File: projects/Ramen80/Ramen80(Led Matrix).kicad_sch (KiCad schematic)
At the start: 113 parts, among them U2 IS31FL3733-TQ, U3 IS31FL3733-TQ

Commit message: Fixing the broke stuff
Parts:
- C10, C14, C8: value 0.1f -> 0.47f
- C13, C5, C9: value 0.47f -> 0.1u
- C15, C18, C7: value 0.47f -> 0.1f
- C16: value 0.1f -> 1u
- C4: value 0.1f -> 4.7u
- R1: value 100k -> 5k1
- R2: value 20k -> 22
- R3: value 2k -> 5k1
- R4: value 2k -> 22
- R5: value 100k -> 10k
- R6: value 20k -> 10k
- renumbered LED18 to LED10, LED19 to LED11, LED20 to LED12, LED21 to LED13, LED22 to LED14, LED23 to LED15, LED24 to LED16, LED34 to LED17, LED35 to LED18, LED36 to LED19, LED37 to LED20, LED38 to LED21, LED39 to LED22, LED40 to LED23, LED41 to LED24, LED51 to LED25, LED52 to LED26, LED53 to LED27, LED54 to LED28, LED55 to LED29, LED56 to LED30, LED57 to LED31, LED58 to LED32, LED64 to LED33, LED65 to LED34, LED66 to LED35, LED67 to LED36, LED68 to LED37, LED69 to LED38, LED70 to LED39, LED71 to LED40, LED77 to LED41, LED78 to LED42, LED79 to LED43, LED80 to LED44, LED9 to LED45, LED10 to LED46, LED11 to LED47, LED12 to LED48, LED13 to LED49, LED14 to LED50, LED15 to LED51, LED16 to LED52, LED25 to LED53, LED26 to LED54, LED27 to LED55, LED28 to LED56, LED29 to LED57, LED30 to LED58, LED31 to LED59, LED32 to LED60, LED42 to LED61, LED43 to LED62, LED44 to LED63, LED45 to LED64, LED46 to LED65, LED47 to LED66, LED48 to LED67, LED49 to LED68, LED59 to LED69, LED60 to LED70, LED61 to LED71, LED62 to LED72, LED63 to LED73, LED33 to LED74, LED50 to LED75, LED72 to LED76, LED73 to LED77, LED74 to LED78, LED75 to LED79, LED76 to LED80, LED17 to LED9

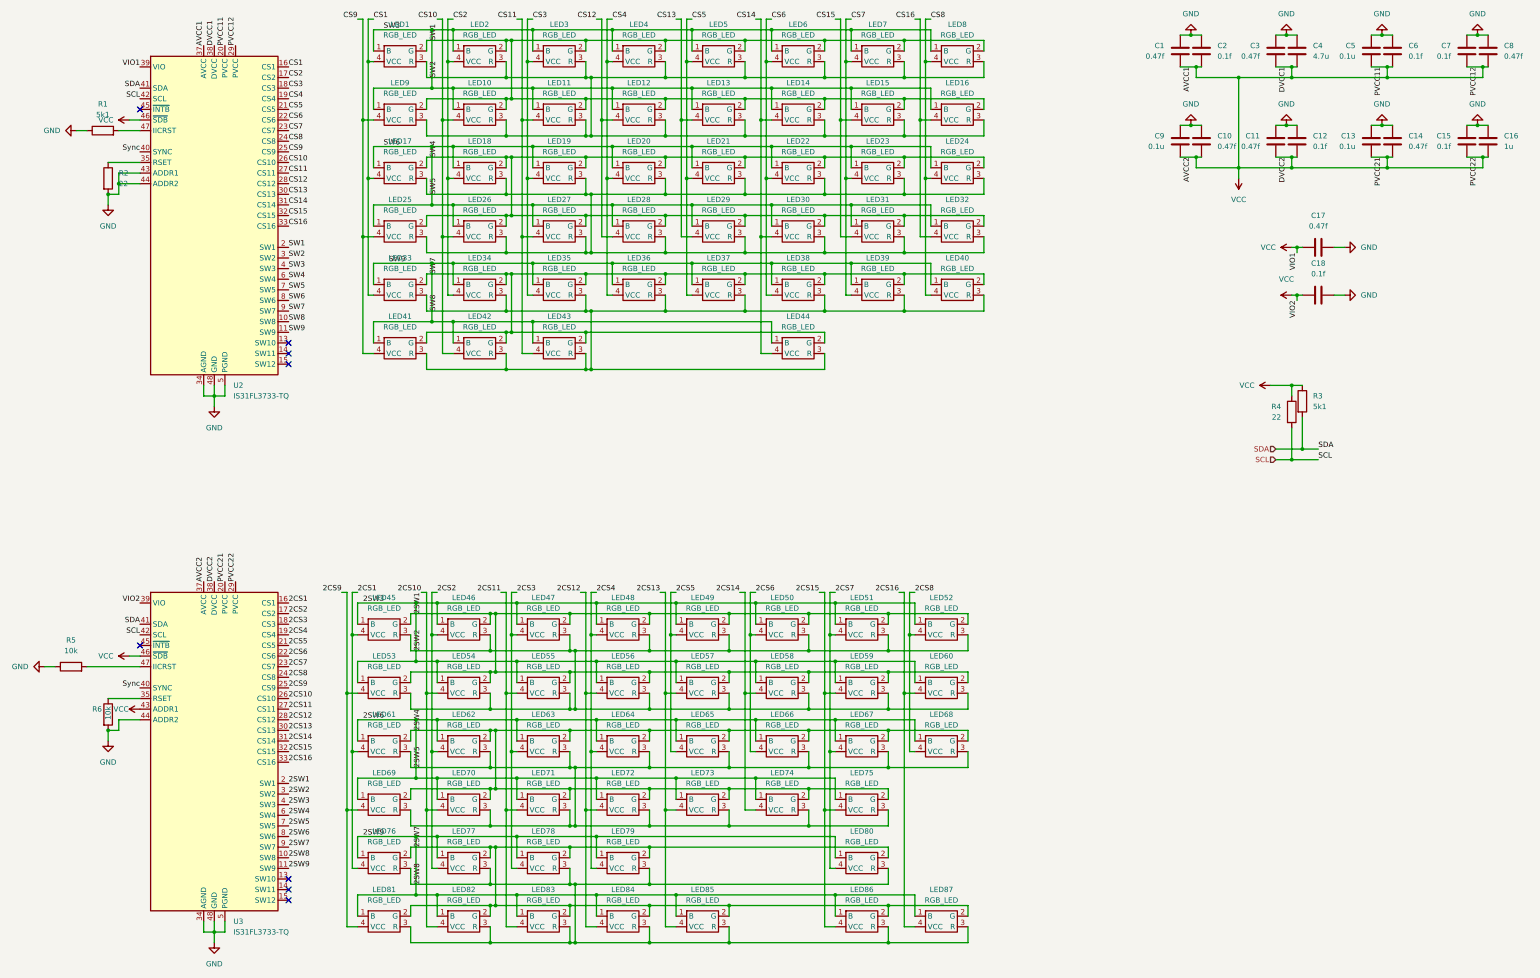
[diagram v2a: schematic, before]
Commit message: Fixes (re-mapped pinout)
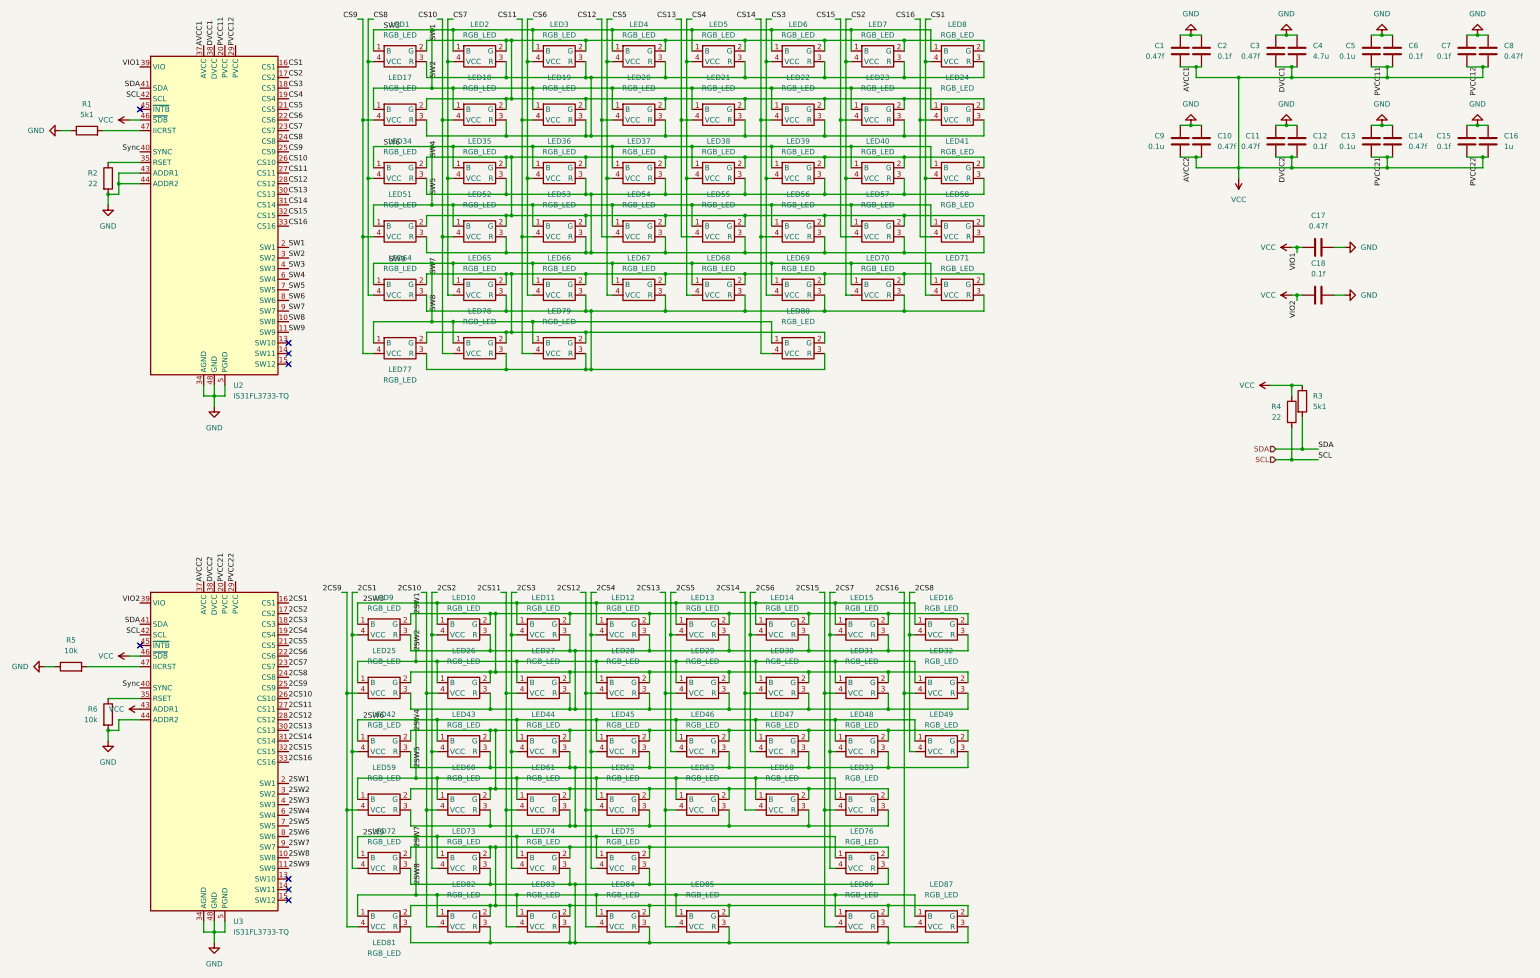
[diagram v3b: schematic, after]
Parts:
- removed LED17, LED18, LED19, LED20, LED21, LED22, LED23, LED24: RGB_LED, RamenKeebs:QBLP677R-RGB, symbol RamenKeebs:RGB_LED
- added LED10, LED11, LED12, LED13, LED14, LED15, LED16, LED9: RGB_LED, RamenKeebs:QBLP677R-RGB, symbol RamenKeebs:RGB_LED
- renumbered LED9 to LED17, LED10 to LED18, LED11 to LED19, LED12 to LED20, LED13 to LED21, LED14 to LED22, LED15 to LED23, LED16 to LED24
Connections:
- net 2CS1: now also LED42.4 (VCC), LED72.4 (VCC), LED9.4 (VCC); no longer LED45.4 (VCC), LED61.4 (VCC), LED76.4 (VCC)
- net 2CS10: now also LED26.4 (VCC), LED60.4 (VCC); no longer LED54.4 (VCC), LED70.4 (VCC)
- net 2CS11: now also LED27.4 (VCC), LED61.4 (VCC); no longer LED55.4 (VCC), LED71.4 (VCC)
- net 2CS12: now also LED28.4 (VCC), LED62.4 (VCC); no longer LED56.4 (VCC), LED72.4 (VCC)
- net 2CS13: now also LED29.4 (VCC), LED63.4 (VCC); no longer LED57.4 (VCC), LED73.4 (VCC)
- net 2CS14: now also LED30.4 (VCC), LED50.4 (VCC); no longer LED58.4 (VCC), LED74.4 (VCC)
- net 2CS15: now also LED31.4 (VCC), LED33.4 (VCC); no longer LED59.4 (VCC), LED75.4 (VCC)
- net 2CS16: now also LED32.4 (VCC); no longer LED60.4 (VCC)
- net 2CS2: now also LED43.4 (VCC), LED73.4 (VCC), LED10.4 (VCC); no longer LED46.4 (VCC), LED62.4 (VCC), LED77.4 (VCC)
- net 2CS3: now also LED44.4 (VCC), LED74.4 (VCC), LED11.4 (VCC); no longer LED47.4 (VCC), LED63.4 (VCC), LED78.4 (VCC)
- net 2CS4: now also LED45.4 (VCC), LED75.4 (VCC), LED12.4 (VCC); no longer LED48.4 (VCC), LED64.4 (VCC), LED79.4 (VCC)
- net 2CS5: now also LED46.4 (VCC), LED13.4 (VCC); no longer LED49.4 (VCC), LED65.4 (VCC)
- net 2CS6: now also LED47.4 (VCC), LED14.4 (VCC); no longer LED50.4 (VCC), LED66.4 (VCC)
- net 2CS7: now also LED48.4 (VCC), LED76.4 (VCC), LED15.4 (VCC); no longer LED51.4 (VCC), LED67.4 (VCC), LED80.4 (VCC)
- net 2CS8: now also LED49.4 (VCC), LED16.4 (VCC); no longer LED52.4 (VCC), LED68.4 (VCC)
- net 2CS9 : now also LED25.4 (VCC), LED59.4 (VCC); no longer LED53.4 (VCC), LED69.4 (VCC)
- net 2SW1: now also LED25.2 (G), LED26.2 (G), LED27.2 (G), LED28.2 (G), LED29.2 (G), LED30.2 (G), LED31.2 (G), LED32.2 (G), LED10.2 (G), LED11.2 (G), LED12.2 (G), LED13.2 (G), LED14.2 (G), LED15.2 (G), LED16.2 (G), LED9.2 (G); no longer LED45.2 (G), LED46.2 (G), LED47.2 (G), LED48.2 (G), LED49.2 (G), LED50.2 (G), LED51.2 (G), LED52.2 (G), LED53.2 (G), LED54.2 (G), LED55.2 (G), LED56.2 (G), LED57.2 (G), LED58.2 (G), LED59.2 (G), LED60.2 (G)
- net 2SW2: now also LED25.3 (R), LED26.3 (R), LED27.3 (R), LED28.3 (R), LED29.3 (R), LED30.3 (R), LED31.3 (R), LED32.3 (R), LED10.3 (R), LED11.3 (R), LED12.3 (R), LED13.3 (R), LED14.3 (R), LED15.3 (R), LED16.3 (R), LED9.3 (R); no longer LED45.3 (R), LED46.3 (R), LED47.3 (R), LED48.3 (R), LED49.3 (R), LED50.3 (R), LED51.3 (R), LED52.3 (R), LED53.3 (R), LED54.3 (R), LED55.3 (R), LED56.3 (R), LED57.3 (R), LED58.3 (R), LED59.3 (R), LED60.3 (R)
- net 2SW3: now also LED25.1 (B), LED26.1 (B), LED27.1 (B), LED28.1 (B), LED29.1 (B), LED30.1 (B), LED31.1 (B), LED32.1 (B), LED10.1 (B), LED11.1 (B), LED12.1 (B), LED13.1 (B), LED14.1 (B), LED15.1 (B), LED16.1 (B), LED9.1 (B); no longer LED45.1 (B), LED46.1 (B), LED47.1 (B), LED48.1 (B), LED49.1 (B), LED50.1 (B), LED51.1 (B), LED52.1 (B), LED53.1 (B), LED54.1 (B), LED55.1 (B), LED56.1 (B), LED57.1 (B), LED58.1 (B), LED59.1 (B), LED60.1 (B)
- net 2SW4: now also LED33.2 (G), LED42.2 (G), LED43.2 (G), LED44.2 (G), LED45.2 (G), LED46.2 (G), LED47.2 (G), LED48.2 (G), LED49.2 (G), LED50.2 (G), LED59.2 (G), LED60.2 (G); no longer LED64.2 (G), LED65.2 (G), LED66.2 (G), LED67.2 (G), LED68.2 (G), LED69.2 (G), LED70.2 (G), LED71.2 (G), LED72.2 (G), LED73.2 (G), LED74.2 (G), LED75.2 (G)
- net 2SW5: now also LED33.3 (R), LED42.3 (R), LED43.3 (R), LED44.3 (R), LED45.3 (R), LED46.3 (R), LED47.3 (R), LED48.3 (R), LED49.3 (R), LED50.3 (R), LED59.3 (R), LED60.3 (R); no longer LED64.3 (R), LED65.3 (R), LED66.3 (R), LED67.3 (R), LED68.3 (R), LED69.3 (R), LED70.3 (R), LED71.3 (R), LED72.3 (R), LED73.3 (R), LED74.3 (R), LED75.3 (R)
- net 2SW6: now also LED33.1 (B), LED42.1 (B), LED43.1 (B), LED44.1 (B), LED45.1 (B), LED46.1 (B), LED47.1 (B), LED48.1 (B), LED49.1 (B), LED50.1 (B), LED59.1 (B), LED60.1 (B); no longer LED64.1 (B), LED65.1 (B), LED66.1 (B), LED67.1 (B), LED68.1 (B), LED69.1 (B), LED70.1 (B), LED71.1 (B), LED72.1 (B), LED73.1 (B), LED74.1 (B), LED75.1 (B)
- net 2SW7: now also LED72.2 (G), LED73.2 (G), LED74.2 (G), LED75.2 (G); no longer LED77.2 (G), LED78.2 (G), LED79.2 (G), LED80.2 (G)
- net 2SW8: now also LED72.3 (R), LED73.3 (R), LED74.3 (R), LED75.3 (R); no longer LED77.3 (R), LED78.3 (R), LED79.3 (R), LED80.3 (R)
- net 2SW9: now also LED72.1 (B), LED73.1 (B), LED74.1 (B), LED75.1 (B); no longer LED77.1 (B), LED78.1 (B), LED79.1 (B), LED80.1 (B)
- net CS1: now also LED41.4 (VCC), LED71.4 (VCC), LED8.4 (VCC); no longer LED1.4 (VCC), LED33.4 (VCC)
- net CS10: now also LED52.4 (VCC), LED78.4 (VCC); no longer LED26.4 (VCC), LED42.4 (VCC)
- net CS11: now also LED53.4 (VCC), LED79.4 (VCC); no longer LED27.4 (VCC), LED43.4 (VCC)
- net CS12: now also LED54.4 (VCC); no longer LED28.4 (VCC)
- net CS13: now also LED55.4 (VCC); no longer LED29.4 (VCC)
- net CS14: now also LED56.4 (VCC), LED80.4 (VCC); no longer LED30.4 (VCC), LED44.4 (VCC)
- net CS15: now also LED57.4 (VCC); no longer LED31.4 (VCC)
- net CS16: now also LED58.4 (VCC); no longer LED32.4 (VCC)
- net CS2: now also LED40.4 (VCC), LED7.4 (VCC), LED70.4 (VCC); no longer LED2.4 (VCC), LED34.4 (VCC)
- net CS3: now also LED39.4 (VCC), LED6.4 (VCC), LED69.4 (VCC); no longer LED3.4 (VCC), LED35.4 (VCC)
- net CS4: now also LED38.4 (VCC), LED5.4 (VCC), LED68.4 (VCC); no longer LED36.4 (VCC), LED4.4 (VCC)
- net CS5: now also LED4.4 (VCC), LED67.4 (VCC); no longer LED5.4 (VCC)
- net CS6: now also LED3.4 (VCC), LED36.4 (VCC), LED66.4 (VCC); no longer LED38.4 (VCC), LED6.4 (VCC)
- net CS7: now also LED2.4 (VCC), LED35.4 (VCC), LED65.4 (VCC); no longer LED39.4 (VCC), LED7.4 (VCC)
- net CS8: now also LED1.4 (VCC), LED34.4 (VCC), LED64.4 (VCC); no longer LED40.4 (VCC), LED8.4 (VCC)
- net CS9 : now also LED51.4 (VCC), LED77.4 (VCC); no longer LED25.4 (VCC), LED41.4 (VCC)
- net SW4: now also LED34.2 (G), LED35.2 (G), LED36.2 (G), LED37.2 (G), LED38.2 (G), LED39.2 (G), LED40.2 (G), LED41.2 (G), LED51.2 (G), LED52.2 (G), LED53.2 (G), LED54.2 (G), LED55.2 (G), LED56.2 (G), LED57.2 (G), LED58.2 (G); no longer LED25.2 (G), LED26.2 (G), LED27.2 (G), LED28.2 (G), LED29.2 (G), LED30.2 (G), LED31.2 (G), LED32.2 (G)
- net SW5: now also LED34.3 (R), LED35.3 (R), LED36.3 (R), LED37.3 (R), LED38.3 (R), LED39.3 (R), LED40.3 (R), LED41.3 (R), LED51.3 (R), LED52.3 (R), LED53.3 (R), LED54.3 (R), LED55.3 (R), LED56.3 (R), LED57.3 (R), LED58.3 (R); no longer LED25.3 (R), LED26.3 (R), LED27.3 (R), LED28.3 (R), LED29.3 (R), LED30.3 (R), LED31.3 (R), LED32.3 (R)
- net SW6: now also LED34.1 (B), LED35.1 (B), LED36.1 (B), LED37.1 (B), LED38.1 (B), LED39.1 (B), LED40.1 (B), LED41.1 (B), LED51.1 (B), LED52.1 (B), LED53.1 (B), LED54.1 (B), LED55.1 (B), LED56.1 (B), LED57.1 (B), LED58.1 (B); no longer LED25.1 (B), LED26.1 (B), LED27.1 (B), LED28.1 (B), LED29.1 (B), LED30.1 (B), LED31.1 (B), LED32.1 (B)
- net SW7: now also LED64.2 (G), LED65.2 (G), LED66.2 (G), LED67.2 (G), LED68.2 (G), LED69.2 (G), LED70.2 (G), LED71.2 (G), LED77.2 (G), LED78.2 (G), LED79.2 (G), LED80.2 (G); no longer LED33.2 (G), LED34.2 (G), LED35.2 (G), LED36.2 (G), LED37.2 (G), LED38.2 (G), LED39.2 (G), LED40.2 (G), LED41.2 (G), LED42.2 (G), LED43.2 (G), LED44.2 (G)
- net SW8: now also LED64.3 (R), LED65.3 (R), LED66.3 (R), LED67.3 (R), LED68.3 (R), LED69.3 (R), LED70.3 (R), LED71.3 (R), LED77.3 (R), LED78.3 (R), LED79.3 (R), LED80.3 (R); no longer LED33.3 (R), LED34.3 (R), LED35.3 (R), LED36.3 (R), LED37.3 (R), LED38.3 (R), LED39.3 (R), LED40.3 (R), LED41.3 (R), LED42.3 (R), LED43.3 (R), LED44.3 (R)
- net SW9 : now also LED64.1 (B), LED65.1 (B), LED66.1 (B), LED67.1 (B), LED68.1 (B), LED69.1 (B), LED70.1 (B), LED71.1 (B), LED77.1 (B), LED78.1 (B), LED79.1 (B), LED80.1 (B); no longer LED33.1 (B), LED34.1 (B), LED35.1 (B), LED36.1 (B), LED37.1 (B), LED38.1 (B), LED39.1 (B), LED40.1 (B), LED41.1 (B), LED42.1 (B), LED43.1 (B), LED44.1 (B)
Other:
- moved on the sheet: R1

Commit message: Final Fixes
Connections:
- net 2CS1: now also LED16.4 (VCC), LED49.4 (VCC); no longer LED42.4 (VCC), LED72.4 (VCC), LED9.4 (VCC)
- net 2CS10: now also LED30.4 (VCC), LED50.4 (VCC); no longer LED26.4 (VCC), LED60.4 (VCC), LED82.4 (VCC)
- net 2CS12: now also LED29.4 (VCC), LED63.4 (VCC), LED85.4 (VCC); no longer LED28.4 (VCC), LED62.4 (VCC), LED84.4 (VCC)
- net 2CS13: now also LED26.4 (VCC), LED60.4 (VCC), LED82.4 (VCC); no longer LED29.4 (VCC), LED63.4 (VCC), LED85.4 (VCC)
- net 2CS14: now also LED31.4 (VCC), LED33.4 (VCC), LED86.4 (VCC); no longer LED30.4 (VCC), LED50.4 (VCC)
- net 2CS15: now also LED25.4 (VCC), LED59.4 (VCC), LED81.4 (VCC); no longer LED31.4 (VCC), LED33.4 (VCC), LED86.4 (VCC)
- net 2CS2: now also LED11.4 (VCC), LED44.4 (VCC), LED74.4 (VCC); no longer LED10.4 (VCC), LED43.4 (VCC), LED73.4 (VCC)
- net 2CS3: now also LED15.4 (VCC), LED48.4 (VCC), LED76.4 (VCC); no longer LED11.4 (VCC), LED44.4 (VCC), LED74.4 (VCC)
- net 2CS4: now also LED14.4 (VCC), LED47.4 (VCC); no longer LED12.4 (VCC), LED45.4 (VCC), LED75.4 (VCC)
- net 2CS5: now also LED10.4 (VCC), LED43.4 (VCC), LED73.4 (VCC); no longer LED13.4 (VCC), LED46.4 (VCC)
- net 2CS6: now also LED13.4 (VCC), LED46.4 (VCC); no longer LED14.4 (VCC), LED47.4 (VCC)
- net 2CS7: now also LED12.4 (VCC), LED45.4 (VCC), LED75.4 (VCC); no longer LED15.4 (VCC), LED48.4 (VCC), LED76.4 (VCC)
- net 2CS8: now also LED42.4 (VCC), LED72.4 (VCC), LED9.4 (VCC); no longer LED16.4 (VCC), LED49.4 (VCC)
- net 2CS9 : now also LED28.4 (VCC), LED62.4 (VCC), LED84.4 (VCC); no longer LED25.4 (VCC), LED59.4 (VCC), LED81.4 (VCC)
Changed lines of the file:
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@@
     (effects (font (size 1.27 1.27)) (justify left bottom))
+  )
+  (label "2CS9 " (at 173.99 177.8 180)
+    (effects (font (size 1.27 1.27)) (justify right bottom))
   )
   (label "CS1" (at 257.81 40.64 0)
@@
     (effects (font (size 1.27 1.27)) (justify right bottom))
   )
+  (label "2CS6" (at 196.85 177.8 0)
+    (effects (font (size 1.27 1.27)) (justify left bottom))
+  )
+  (label "2CS13" (at 135.89 177.8 180)
+    (effects (font (size 1.27 1.27)) (justify right bottom))
+  )
+  (label "2CS1" (at 254 177.8 0)
+    (effects (font (size 1.27 1.27)) (justify left bottom))
+  )
   (label "PVCC11" (at 88.9 46.99 90)
     (effects (font (size 1.27 1.27)) (justify left bottom))
@@
     (effects (font (size 1.27 1.27)) (justify right bottom))
   )
+  (label "2CS7" (at 177.8 177.8 0)
+    (effects (font (size 1.27 1.27)) (justify left bottom))
+  )
   (label "CS10" (at 139.7 40.64 180)
     (effects (font (size 1.27 1.27)) (justify right bottom))
@@
     (effects (font (size 1.27 1.27)) (justify left bottom))
   )
-  (label "2CS1" (at 120.65 177.8 0)
-    (effects (font (size 1.27 1.27)) (justify left bottom))
-  )
   (label "2CS7" (at 104.14 195.58 0)
     (effects (font (size 1.27 1.27)) (justify left bottom))
@@
     (effects (font (size 1.27 1.27)) (justify left bottom))
   )
+  (label "2CS10" (at 212.09 177.8 180)
+    (effects (font (size 1.27 1.27)) (justify right bottom))
+  )
   (label "PVCC22" (at 91.44 175.26 90)
     (effects (font (size 1.27 1.27)) (justify left bottom))
@@
     (effects (font (size 1.27 1.27)) (justify left bottom))
   )
+  (label "2CS12" (at 193.04 177.8 180)
+    (effects (font (size 1.27 1.27)) (justify right bottom))
+  )
   (label "CS16" (at 254 40.64 180)
     (effects (font (size 1.27 1.27)) (justify right bottom))
   )
-  (label "2CS9 " (at 116.84 177.8 180)
-    (effects (font (size 1.27 1.27)) (justify right bottom))
-  )
   (label "CS15" (at 234.95 40.64 180)
     (effects (font (size 1.27 1.27)) (justify right bottom))
@@
     (effects (font (size 1.27 1.27)) (justify right bottom))
   )
-  (label "2CS12" (at 173.99 177.8 180)
-    (effects (font (size 1.27 1.27)) (justify right bottom))
+  (label "2CS3" (at 234.95 177.8 0)
+    (effects (font (size 1.27 1.27)) (justify left bottom))
   )
   (label "2SW6" (at 127 208.28 180)
@@
     (effects (font (size 1.27 1.27)) (justify left bottom))
   )
-  (label "2CS7" (at 234.95 177.8 0)
-    (effects (font (size 1.27 1.27)) (justify left bottom))
-  )
   (label "CS11" (at 104.14 77.47 0)
     (effects (font (size 1.27 1.27)) (justify left bottom))
   )
-  (label "2CS5" (at 196.85 177.8 0)
-    (effects (font (size 1.27 1.27)) (justify left bottom))
-  )
   (label "SW3" (at 130.81 43.18 180)
     (effects (font (size 1.27 1.27)) (justify right bottom))
@@
     (effects (font (size 1.27 1.27)) (justify left bottom))
   )
-  (label "2CS8" (at 254 177.8 0)
-    (effects (font (size 1.27 1.27)) (justify left bottom))
-  )
   (label "2CS11" (at 104.14 205.74 0)
     (effects (font (size 1.27 1.27)) (justify left bottom))
   )
+  (label "2CS5" (at 139.7 177.8 0)
+    (effects (font (size 1.27 1.27)) (justify left bottom))
+  )
   (label "2CS15" (at 104.14 215.9 0)
     (effects (font (size 1.27 1.27)) (justify left bottom))
@@
     (effects (font (size 1.27 1.27)) (justify left bottom))
   )
+  (label "2CS15" (at 116.84 177.8 180)
+    (effects (font (size 1.27 1.27)) (justify right bottom))
+  )
   (label "2SW4" (at 135.89 210.82 90)
     (effects (font (size 1.27 1.27)) (justify left bottom))
@@
     (effects (font (size 1.27 1.27)) (justify left bottom))
   )
+  (label "2CS11" (at 154.94 177.8 180)
+    (effects (font (size 1.27 1.27)) (justify right bottom))
+  )
   (label "2SW3" (at 127 180.34 180)
     (effects (font (size 1.27 1.27)) (justify right bottom))
@@
     (effects (font (size 1.27 1.27)) (justify right bottom))
   )
-  (label "2CS4" (at 177.8 177.8 0)
-    (effects (font (size 1.27 1.27)) (justify left bottom))
-  )
   (label "2SW7" (at 104.14 238.76 0)
     (effects (font (size 1.27 1.27)) (justify left bottom))
@@
     (effects (font (size 1.27 1.27)) (justify left bottom))
   )
-  (label "2CS6" (at 215.9 177.8 0)
-    (effects (font (size 1.27 1.27)) (justify left bottom))
-  )
   (label "SW7" (at 139.7 101.6 90)
     (effects (font (size 1.27 1.27)) (justify left bottom))
@@
     (effects (font (size 1.27 1.27)) (justify left bottom))
   )
-  (label "2CS10" (at 135.89 177.8 180)
-    (effects (font (size 1.27 1.27)) (justify right bottom))
-  )
   (label "PVCC21" (at 88.9 175.26 90)
     (effects (font (size 1.27 1.27)) (justify left bottom))
@@
     (effects (font (size 1.27 1.27)) (justify left bottom))
   )
+  (label "2CS2" (at 158.75 177.8 0)
+    (effects (font (size 1.27 1.27)) (justify left bottom))
+  )
   (label "2SW4" (at 104.14 231.14 0)
     (effects (font (size 1.27 1.27)) (justify left bottom))
@@
     (effects (font (size 1.27 1.27)) (justify left bottom))
   )
+  (label "2CS4" (at 215.9 177.8 0)
+    (effects (font (size 1.27 1.27)) (justify left bottom))
+  )
   (label "CS15" (at 104.14 87.63 0)
     (effects (font (size 1.27 1.27)) (justify left bottom))
@@
     (effects (font (size 1.27 1.27)) (justify right bottom))
   )
-  (label "2CS11" (at 154.94 177.8 180)
-    (effects (font (size 1.27 1.27)) (justify right bottom))
-  )
   (label "SW4" (at 104.14 102.87 0)
     (effects (font (size 1.27 1.27)) (justify left bottom))
@@
     (effects (font (size 1.27 1.27)) (justify left bottom))
   )
-  (label "2CS3" (at 158.75 177.8 0)
-    (effects (font (size 1.27 1.27)) (justify left bottom))
-  )
-  (label "2CS2" (at 139.7 177.8 0)
-    (effects (font (size 1.27 1.27)) (justify left bottom))
-  )
   (label "CS5" (at 181.61 40.64 0)
     (effects (font (size 1.27 1.27)) (justify left bottom))
@@
     (effects (font (size 1.27 1.27)) (justify left bottom))
   )
+  (label "2CS8" (at 120.65 177.8 0)
+    (effects (font (size 1.27 1.27)) (justify left bottom))
+  )
   (label "CS1" (at 104.14 52.07 0)
     (effects (font (size 1.27 1.27)) (justify left bottom))
   )
-  (label "2CS14" (at 212.09 177.8 180)
-    (effects (font (size 1.27 1.27)) (justify right bottom))
-  )
   (label "2CS5" (at 104.14 190.5 0)
     (effects (font (size 1.27 1.27)) (justify left bottom))
@@
     (effects (font (size 1.27 1.27)) (justify left bottom))
   )
-  (label "2CS15" (at 231.14 177.8 180)
-    (effects (font (size 1.27 1.27)) (justify right bottom))
-  )
-  (label "2CS13" (at 193.04 177.8 180)
-    (effects (font (size 1.27 1.27)) (justify right bottom))
-  )
   (label "VIO1" (at 345.44 96.52 270)
     (effects (font (size 1.27 1.27)) (justify right bottom))
@@
     (effects (font (size 1.27 1.27)) (justify left bottom))
   )
+  (label "2CS14" (at 231.14 177.8 180)
+    (effects (font (size 1.27 1.27)) (justify right bottom))
+  )
   (label "CS11" (at 158.75 40.64 180)
